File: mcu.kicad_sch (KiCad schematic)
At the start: 36 parts

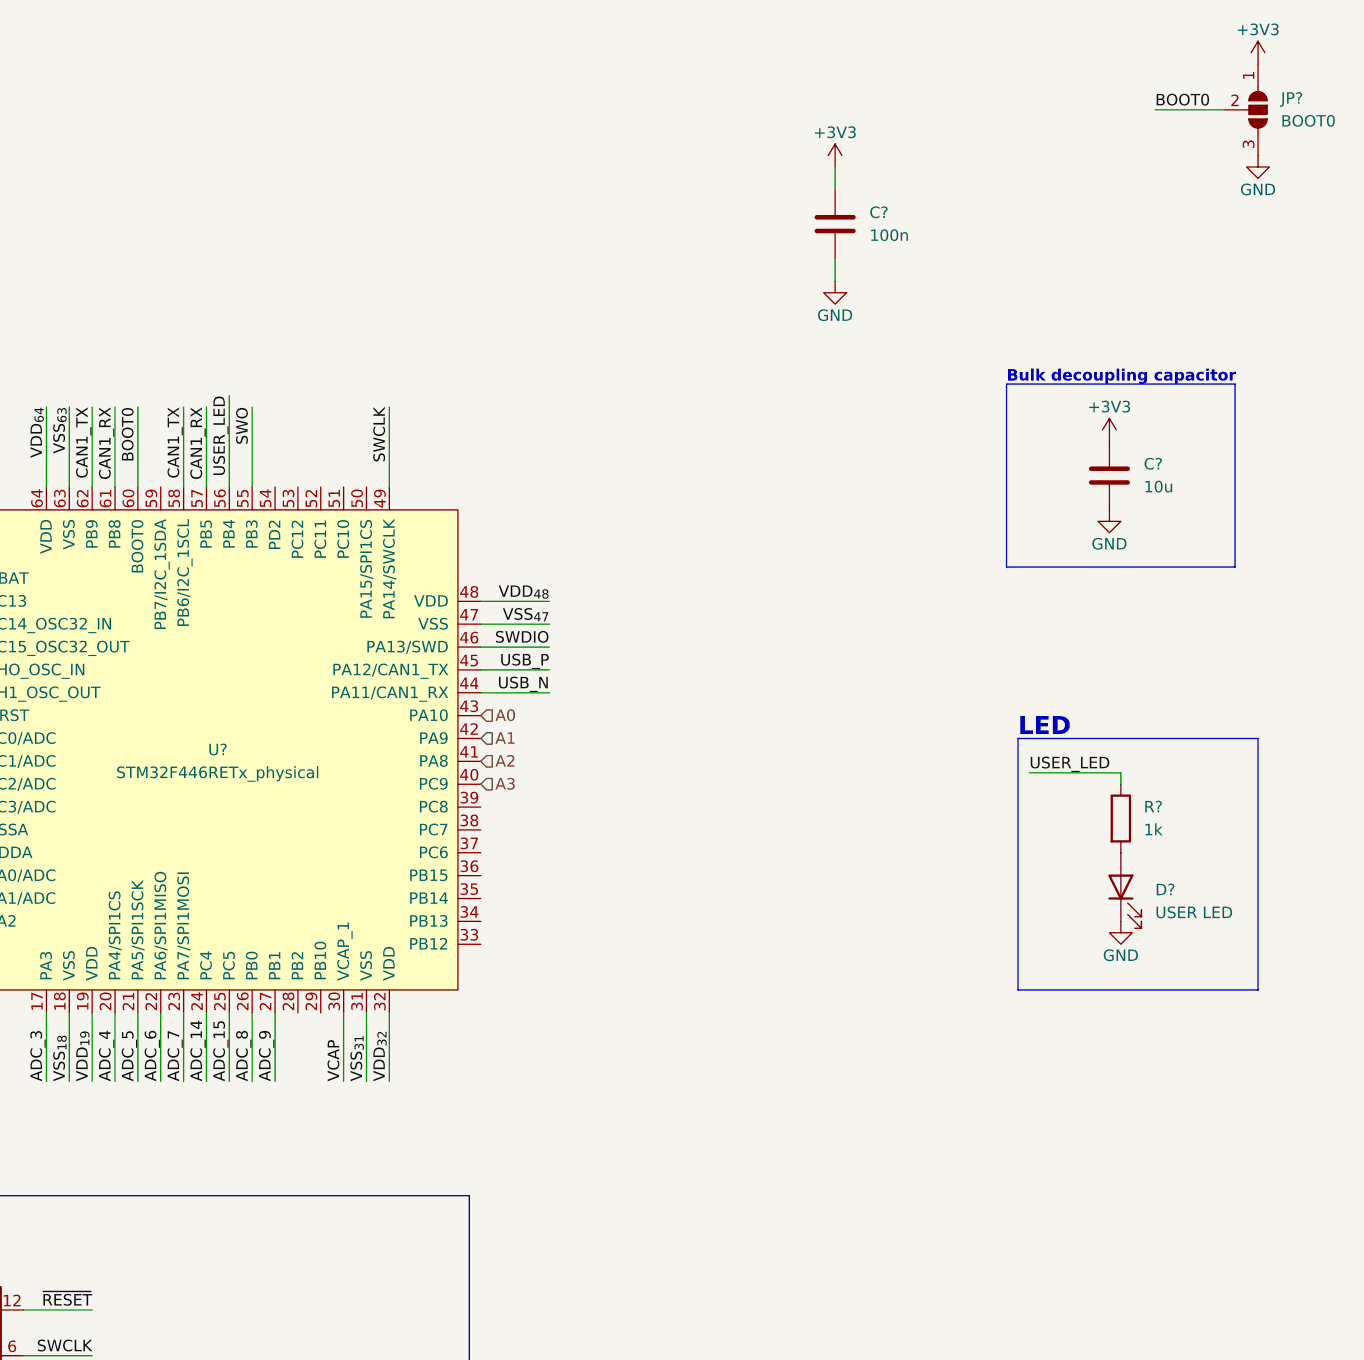
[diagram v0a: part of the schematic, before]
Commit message: sch: add opamps
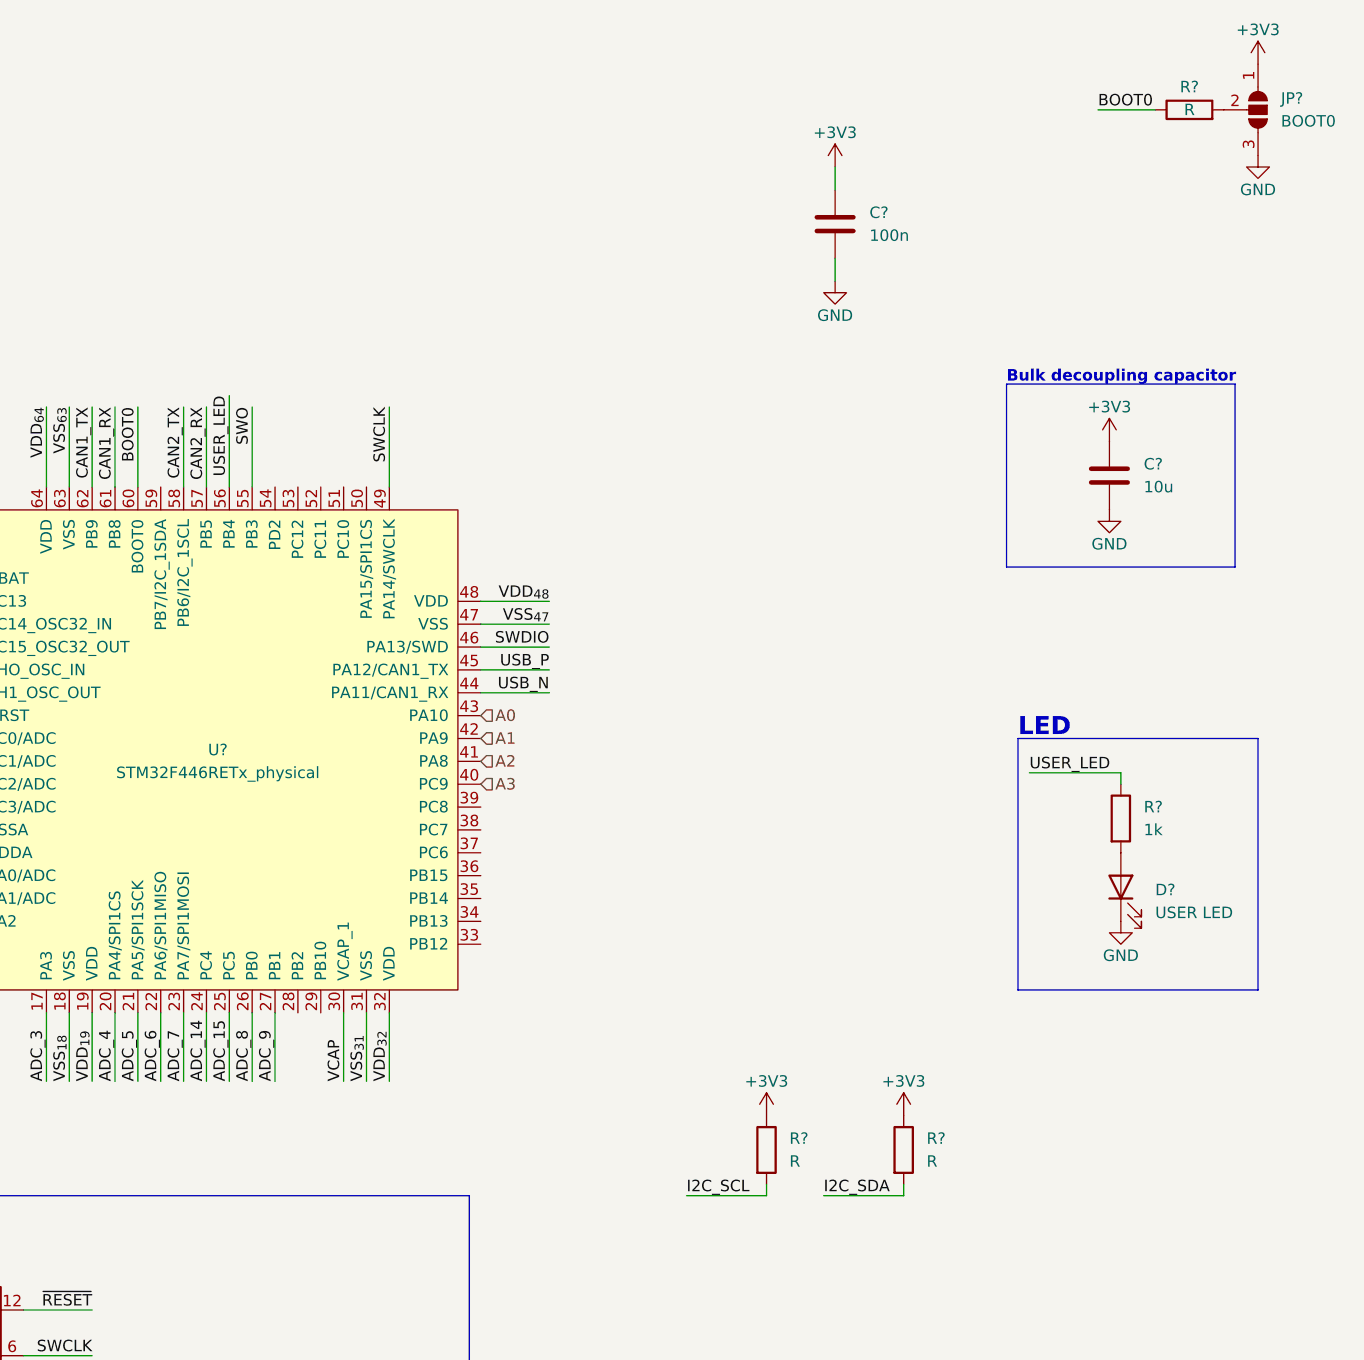
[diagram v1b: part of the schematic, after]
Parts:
- added R? (x2): R, Resistor_SMD:R_0603_1608Metric, symbol Device:R
- added R?: R, symbol Device:R
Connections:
- net +3V3: now also R?.1, R?.1
- net BOOT0: now also R?.1; no longer JP?.2 (C)
- net CAN1_RX: no longer U?.57 (PB5)
- net CAN1_TX: no longer U?.58 (PB6/I2C_1SCL)
- net CAN2_RX: now also U?.57 (PB5)
- net CAN2_TX: now also U?.58 (PB6/I2C_1SCL)
- new net: JP?.2 (C), R?.2
- new net I2C_SCL: R?.2
- new net I2C_SDA: R?.2
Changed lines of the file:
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@@
     (stroke (width 0) (type default) (color 0 0 0 0))
   )
-  (wire (pts (xy 251.46 22.86) (xy 259.08 22.86))
+  (wire (pts (xy 245.11 22.86) (xy 251.46 22.86))
     (stroke (width 0) (type default) (color 0 0 0 0))
   )
@@
     (stroke (width 0) (type default) (color 0 0 0 0))
   )
+  (wire (pts (xy 223.52 143.51) (xy 223.52 142.24))
+    (stroke (width 0) (type default) (color 0 0 0 0))
+  )
   (wire (pts (xy 130.81 55.88) (xy 130.81 64.77))
     (stroke (width 0) (type default) (color 0 0 0 0))
@@
     (stroke (width 0) (type default) (color 0 0 0 0))
   )
+  (wire (pts (xy 208.28 143.51) (xy 208.28 142.24))
+    (stroke (width 0) (type default) (color 0 0 0 0))
+  )
   (wire (pts (xy -66.04 57.15) (xy -74.93 57.15))
     (stroke (width 0) (type default) (color 0 0 0 0))
@@
     (stroke (width 0) (type default) (color 0 0 0 0))
   )
+  (wire (pts (xy 199.39 143.51) (xy 208.28 143.51))
+    (stroke (width 0) (type default) (color 0 0 0 0))
+  )
   (wire (pts (xy 135.89 130.81) (xy 135.89 123.19))
     (stroke (width 0) (type default) (color 0 0 0 0))
@@
   )
   (polyline (pts (xy 234.95 53.34) (xy 260.35 53.34))
+    (stroke (width 0) (type default) (color 0 0 0 0))
+  )
+  (wire (pts (xy 214.63 143.51) (xy 223.52 143.51))
     (stroke (width 0) (type default) (color 0 0 0 0))
   )
@@
     (effects (font (size 1.27 1.27)) (justify left bottom))
   )
-  (label "BOOT0" (at 251.46 22.86 0)
+  (label "BOOT0" (at 245.11 22.86 0)
     (effects (font (size 1.27 1.27)) (justify left bottom))
   )
@@
     (effects (font (size 1.27 1.27)) (justify right bottom))
   )
-  (label "CAN1_TX" (at 143.51 55.88 270)
+  (label "CAN2_TX" (at 143.51 55.88 270)
     (effects (font (size 1.27 1.27)) (justify right bottom))
   )
@@
     (effects (font (size 1.27 1.27)) (justify left bottom))
   )
-  (label "CAN1_RX" (at 146.05 55.88 270)
+  (label "CAN2_RX" (at 146.05 55.88 270)
     (effects (font (size 1.27 1.27)) (justify right bottom))
   )
@@
     (effects (font (size 1.27 1.27)) (justify right bottom))
   )
+  (label "I2C_SDA" (at 214.63 143.51 0)
+    (effects (font (size 1.27 1.27)) (justify left bottom))
+  )
   (label "SWDIO" (at 184.15 82.55 180)
     (effects (font (size 1.27 1.27)) (justify right bottom))
+  )
+  (label "I2C_SCL" (at 199.39 143.51 0)
+    (effects (font (size 1.27 1.27)) (justify left bottom))
   )
   (hierarchical_label "CAN1-" (shape bidirectional) (at -92.71 67.31 0)
@@
     (pin "2")
   )
+  (symbol (lib_id "Device:R") (at 208.28 138.43 0) (unit 1)
+    (in_bom yes) (on_board yes) (fields_autoplaced)
+    (property "Reference" "R?" (id 0) (at 210.82 137.1599 0)
+      (effects (font (size 1.27 1.27)) (justify left))
+    )
+    (property "Value" "R" (id 1) (at 210.82 139.6999 0)
+      (effects (font (size 1.27 1.27)) (justify left))
+    )
+    (property "Footprint" "Resistor_SMD:R_0603_1608Metric" (id 2) (at 206.502 138.43 90)
+      (effects (font (size 1.27 1.27)) hide)
+    )
+    (property "Datasheet" "~" (id 3) (at 208.28 138.43 0)
+      (effects (font (size 1.27 1.27)) hide)
+    )
+    (pin "1")
+    (pin "2")
+  )
   (symbol (lib_id "Device:C") (at -68.58 124.46 0) (unit 1)
     (in_bom yes) (on_board yes)
@@
     )
     (pin "1")
+  )
+  (symbol (lib_id "Device:R") (at 255.27 22.86 90) (unit 1)
+    (in_bom yes) (on_board yes)
+    (property "Reference" "R?" (id 0) (at 255.27 20.32 90))
+    (property "Value" "R" (id 1) (at 255.27 22.86 90))
+    (property "Footprint" "" (id 2) (at 255.27 24.638 90)
+      (effects (font (size 1.27 1.27)) hide)
+    )
+    (property "Datasheet" "~" (id 3) (at 255.27 22.86 0)
+      (effects (font (size 1.27 1.27)) hide)
+    )
+    (pin "1")
+    (pin "2")
   )
   (symbol (lib_id "Device:Crystal_GND24") (at 36.83 63.5 0) (unit 1)
@@
     (pin "1")
   )
+  (symbol (lib_id "Device:R") (at 223.52 138.43 0) (unit 1)
+    (in_bom yes) (on_board yes) (fields_autoplaced)
+    (property "Reference" "R?" (id 0) (at 226.06 137.1599 0)
+      (effects (font (size 1.27 1.27)) (justify left))
+    )
+    (property "Value" "R" (id 1) (at 226.06 139.6999 0)
+      (effects (font (size 1.27 1.27)) (justify left))
+    )
+    (property "Footprint" "Resistor_SMD:R_0603_1608Metric" (id 2) (at 221.742 138.43 90)
+      (effects (font (size 1.27 1.27)) hide)
+    )
+    (property "Datasheet" "~" (id 3) (at 223.52 138.43 0)
+      (effects (font (size 1.27 1.27)) hide)
+    )
+    (pin "1")
+    (pin "2")
+  )
   (symbol (lib_id "power:+3V3") (at 20.32 88.9 0) (unit 1)
     (in_bom yes) (on_board yes)
@@
     (pin "1")
     (pin "2")
+  )
+  (symbol (lib_id "power:+3V3") (at 208.28 134.62 0) (unit 1)
+    (in_bom yes) (on_board yes)
+    (property "Reference" "#PWR?" (id 0) (at 208.28 138.43 0)
+      (effects (font (size 1.27 1.27)) hide)
+    )
+    (property "Value" "+3V3" (id 1) (at 208.28 130.81 0))
+    (property "Footprint" "" (id 2) (at 208.28 134.62 0)
+      (effects (font (size 1.27 1.27)) hide)
+    )
+    (property "Datasheet" "" (id 3) (at 208.28 134.62 0)
+      (effects (font (size 1.27 1.27)) hide)
+    )
+    (pin "1")
   )
   (symbol (lib_id "Eagle_Main:STM32F446RETx_physical") (at 147.32 93.98 0) (unit 1)
@@
       (effects (font (size 1.27 1.27)) hide)
     )
+    (pin "1")
+  )
+  (symbol (lib_id "power:+3V3") (at 223.52 134.62 0) (unit 1)
+    (in_bom yes) (on_board yes)
+    (property "Reference" "#PWR?" (id 0) (at 223.52 138.43 0)
+      (effects (font (size 1.27 1.27)) hide)
+    )
+    (property "Value" "+3V3" (id 1) (at 223.52 130.81 0))
+    (property "Footprint" "" (id 2) (at 223.52 134.62 0)
+      (effects (font (size 1.27 1.27)) hide)
+    )
+    (property "Datasheet" "" (id 3) (at 223.52 134.62 0)
+      (effects (font (size 1.27 1.27)) hide)
+    )

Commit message: sch: change to stm32l432k and change analog input topology
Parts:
- removed C? (x2): C, Resistor_SMD:R_0603_1608Metric, symbol Device:C
- removed C? (x2): 100n, Capacitor_SMD:C_0603_1608Metric, symbol Device:C
- removed C? (x4): C, symbol Device:C
- removed FB?: FerriteBead, symbol Device:FerriteBead_Small
- removed JP?: BOOT0, symbol Jumper:SolderJumper_3_Open
- removed R?: R, symbol Device:R
- removed R?: 1k, Resistor_SMD:R_0603_1608Metric, symbol Device:R
- removed R?: 120, Resistor_SMD:R_0805_2012Metric, symbol Device:R
- removed RN? (x2): 33, Resistor_SMD:R_Array_Convex_4x0603, symbol Device:R_Pack04_Split
- removed U?: STM32F446RETx_physical, symbol Eagle_Main:STM32F446RETx_physical
- removed U?: MCP2562FD, Package_SO:SOIC-8_3.9x4.9mm_P1.27mm, symbol Eagle_Main:MCP2562
- removed Y?: 16MHz, symbol Device:Crystal_GND24
- added C? (x3): 100n, Capacitor_SMD:C_0603_1608Metric, symbol Device:C
- added C?: 1u, Capacitor_SMD:C_0603_1608Metric, symbol Device:C
- added D?: STLINK V3 MINIE, symbol Eagle_Symbols:Datasheet
- added FB?: FerriteBead, symbol Device:FerriteBead_Small
- added JP?: BOOT0, symbol Jumper:SolderJumper_3_Open
- added JP?: USB N, symbol Jumper:SolderJumper_2_Open
- added JP?: USB P, symbol Jumper:SolderJumper_2_Open
- added RN?: R, symbol Device:R_Pack04_Split
- added U?: STM32L432KCUx, Package_DFN_QFN:QFN-32-1EP_5x5mm_P0.5mm_EP3.45x3.45mm, symbol MCU_ST_STM32L4:STM32L432KCUx
- added U?: DSC61XX, symbol Eagle_Main:DSC61XX
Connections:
- net +3.3VA: now also C?.1, C?.1, FB?.2, U?.5 (VDDA)
- net +3V3: now also C?.1, C?.1, FB?.1, JP?.1 (A), U?.1 (OE), U?.1 (VDD), U?.17 (VDD), U?.4 (NRST), U?.4 (VDD)
- net A0: now also U?.26 (PB3)
- net A1: now also U?.27 (PB4)
- net A2: now also U?.28 (PB5)
- net A3: now also U?.25 (PA15)
- net ADC_0: now also U?.7 (PA1)
- net ADC_1: now also U?.8 (PA2)
- net ADC_2: now also U?.9 (PA3)
- net ADC_3: now also U?.10 (PA4)
- net ADC_4: now also U?.11 (PA5)
- net ADC_5: now also U?.12 (PA6)
- net ADC_6: now also U?.13 (PA7)
- net ADC_7: now also U?.14 (PB0)
- net ADC_8: now also U?.15 (PB1)
- net BOOT0: now also RN?.1 (R1.1), U?.31 (PH3)
- net CAN1_RX: now also JP?.1 (A), U?.21 (PA11)
- net CAN1_TX: now also JP?.1 (A), U?.22 (PA12)
- net DBG_RX: now also U?.30 (PB7)
- net DBG_TX: now also U?.29 (PB6)
- net GND: now also C?.2, C?.2, JP?.3 (B), U?.16 (VSS), U?.2 (GND), U?.32 (VSS)
- net GNDA: now also C?.2, C?.2, U?.33 (VSS)
- net I2C_SCL: now also U?.19 (PA9)
- net I2C_SDA: now also U?.20 (PA10)
- net SWCLK: now also U?.24 (PA14)
- net SWDIO: now also U?.23 (PA13)
- net USB_N: now also JP?.2 (B)
- net USB_P: now also JP?.2 (B)
- net USER_LED: now also U?.18 (PA8)
- net SWO: no longer names the net of J?.8 (JTDO/SWO)
- new net: JP?.2 (C), RN?.8 (R1.2)
- new net CLK: U?.3 (OUT), U?.6 (PA0)
- no-connect marks 4 -> 5
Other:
- note added: "BOOT0 Config"
- note added: "CAN"
- note added: "Decoupling"
- note added: "I2C Pullup"
- note added: "MCU"
- note added: "Oscillator"
- note added: "Should use LDO from 5VA?"
- note removed: "Crystal"
- moved on the sheet: C?, D?, R?, RN?C, RN?D, SW?, U?
